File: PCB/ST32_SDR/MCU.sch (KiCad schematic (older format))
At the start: 2 parts

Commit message: add SPI in CubeMX project, add FRAM CPU PCB Project
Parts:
- removed U?: STM32F401RCTx, LQFP64, symbol STM32F401RCTx
- added C? (x4): C_Small, symbol C_Small
- added R? (x2): 0*, symbol R_Small
- added U?: STM32F401RCTx, LQFP64, symbol STM32F401RCTx
- added U?: FM24CL16B, Housings_SOIC:SOIC-8_3.9x4.9mm_Pitch1.27mm, symbol 24LC16
- added Y?: 20Mhz, symbol Crystal
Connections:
- net labels added: GND
- wire segments 30 -> 58

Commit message: Schematics update
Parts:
- removed U?: STM32F405RGTx, LQFP64, symbol STM32F405RGTx
- added C129, C130, C131, C132: 100nF, symbol C_Small
- added R94, R95: 4.7k, symbol R_Small
- C120: renamed from C?; value C_Small -> 100nF
- gave numbers to parts that had none: 8
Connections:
- net labels added: +3V3
- wire segments 58 -> 89
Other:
- moved on the sheet: U17

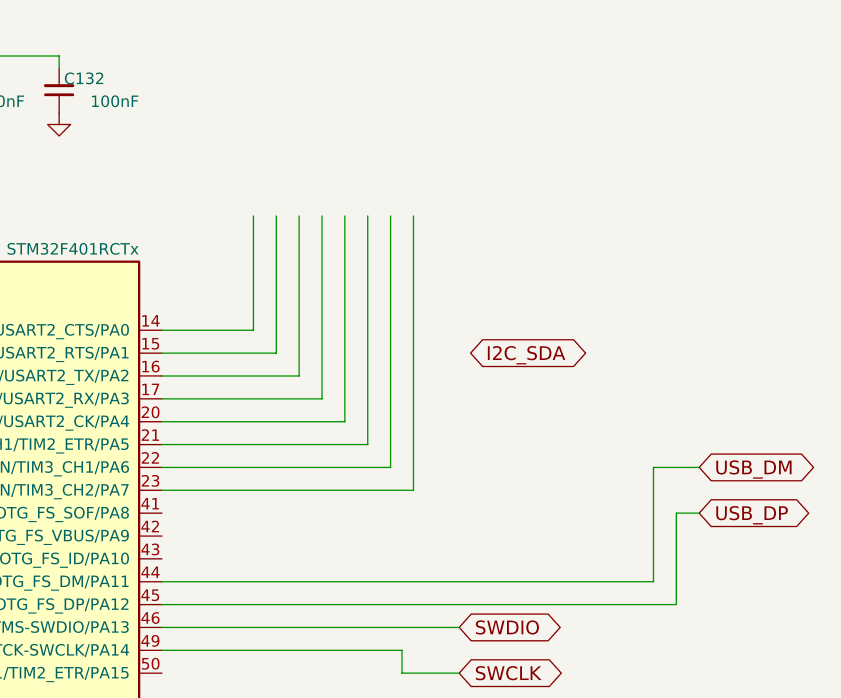
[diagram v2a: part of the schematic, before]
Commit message: MCU schematics updated LCD Interface
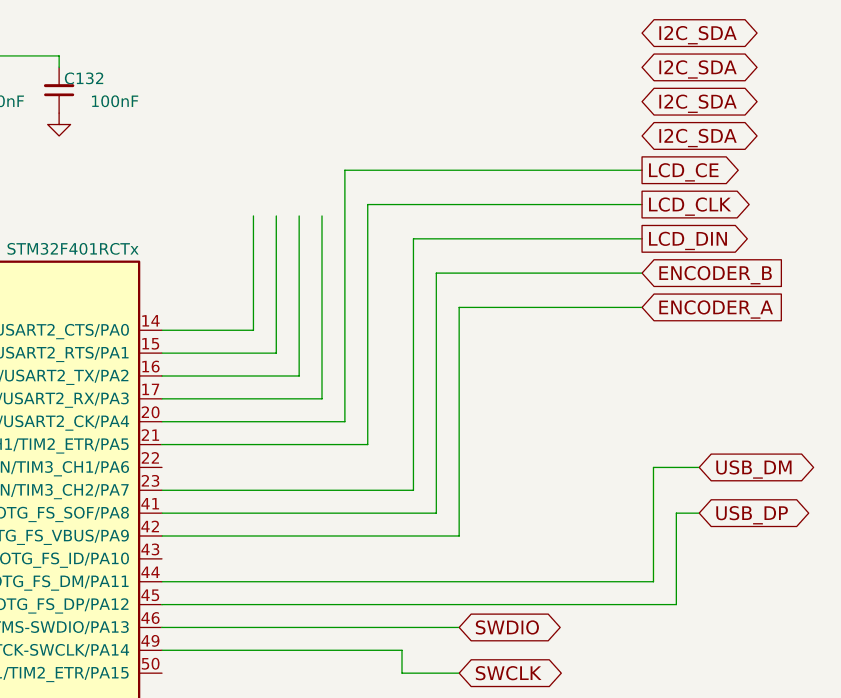
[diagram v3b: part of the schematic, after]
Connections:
- net labels added: ENCODER_A, ENCODER_B, LCD_CE, LCD_CLK, LCD_DIN
- wire segments 89 -> 96
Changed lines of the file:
@@
 LIBS:contrib
 LIBS:LCSDR
-LIBS:Logic_74xx
-LIBS:Logic_CMOS_4000
 LIBS:4ms-ic
-LIBS:Connector
 LIBS:Display
-LIBS:TRXklopik
 LIBS:LCSDR-cache
 EELAYER 25 0
@@
 	1    0    0    -1
 $EndComp
-Text GLabel 9600 1950 2    60   BiDi ~ 0
+Text GLabel 10350 850  2    60   BiDi ~ 0
 I2C_SDA
 Wire Wire Line
@@
 	8950 2150 8950 1350
 Wire Wire Line
-	8250 2250 9050 2250
-Wire Wire Line
-	9050 2250 9050 1350
-Wire Wire Line
-	8250 2350 9150 2350
-Wire Wire Line
-	9150 2350 9150 1350
-Wire Wire Line
-	8250 2450 9250 2450
-Wire Wire Line
-	9250 2450 9250 1350
+	9050 2250 8250 2250
+Wire Wire Line
+	9050 1150 9050 2250
+Wire Wire Line
+	9150 2350 8250 2350
+Wire Wire Line
+	9150 1300 9150 2350
 Wire Wire Line
 	10500 3050 10500 2650
@@
 	10400 2450 10600 2450
 Wire Wire Line
-	8250 2550 9350 2550
-Wire Wire Line
-	9350 2550 9350 1350
+	9350 2550 8250 2550
+Text GLabel 10350 700  2    60   BiDi ~ 0
+I2C_SDA
+Text GLabel 10350 550  2    60   BiDi ~ 0
+I2C_SDA
+Wire Wire Line
+	9050 1150 10350 1150
+Text GLabel 10350 1000 2    60   BiDi ~ 0
+I2C_SDA
+Text GLabel 10350 1150 2    60   Output ~ 0
+LCD_CE
+Text GLabel 10350 1300 2    60   Output ~ 0
+LCD_CLK
+Wire Wire Line
+	10350 1300 9150 1300
+Text GLabel 10350 1450 2    60   Output ~ 0
+LCD_DIN
+Wire Wire Line
+	9350 1450 9350 2550
+Wire Wire Line
+	9350 1450 10350 1450
+Wire Wire Line
+	8250 2650 9450 2650
+Wire Wire Line
+	9450 2650 9450 1600
+Wire Wire Line
+	9450 1600 10350 1600
+Wire Wire Line
+	8250 2750 9550 2750
+Text GLabel 10350 1600 2    60   Input ~ 0
+ENCODER_B
+Text GLabel 10350 1750 2    60   Input ~ 0
+ENCODER_A
+Wire Wire Line
+	10350 1750 9550 1750
+Wire Wire Line
+	9550 1750 9550 2750
 $EndSCHEMATC

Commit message: add LCD resistors
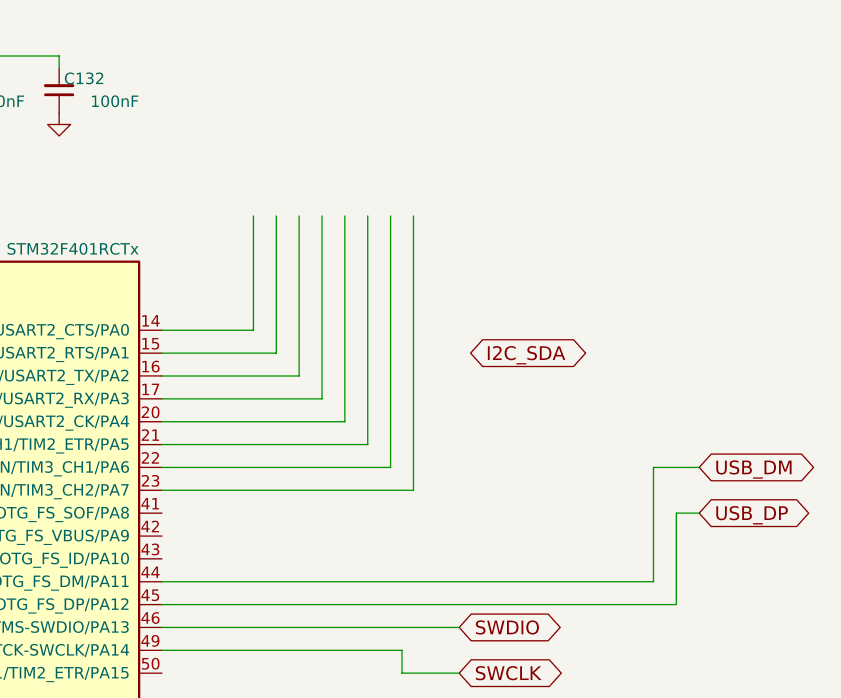
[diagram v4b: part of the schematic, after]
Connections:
- net labels removed: ENCODER_A, ENCODER_B, LCD_CE, LCD_CLK, LCD_DIN
- wire segments 96 -> 89
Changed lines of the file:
@@
 LIBS:contrib
 LIBS:LCSDR
+LIBS:Logic_74xx
+LIBS:Logic_CMOS_4000
 LIBS:4ms-ic
+LIBS:Connector
 LIBS:Display
+LIBS:TRXklopik
 LIBS:LCSDR-cache
 EELAYER 25 0
@@
 $EndComp
 $Comp
-L GND #PWR0168
+L GND #PWR171
 U 1 1 5DD64FC0
 P 5900 5900
-F 0 "#PWR0168" H 5900 5650 50  0001 C CNN
+F 0 "#PWR171" H 5900 5650 50  0001 C CNN
 F 1 "GND" H 5900 5750 50  0001 C CNN
 F 2 "" H 5900 5900 50  0001 C CNN
@@
 	5950 5350 5950 5600
 $Comp
-L GND #PWR0169
+L GND #PWR172
 U 1 1 5DD650F1
 P 6150 5450
-F 0 "#PWR0169" H 6150 5200 50  0001 C CNN
+F 0 "#PWR172" H 6150 5200 50  0001 C CNN
 F 1 "GND" H 6150 5300 50  0001 C CNN
 F 2 "" H 6150 5450 50  0001 C CNN
@@
 Connection ~ 6150 5400
 $Comp
-L GND #PWR0170
+L GND #PWR167
 U 1 1 5DD65332
 P 3250 2700
-F 0 "#PWR0170" H 3250 2450 50  0001 C CNN
+F 0 "#PWR167" H 3250 2450 50  0001 C CNN
 F 1 "GND" H 3250 2550 50  0001 C CNN
 F 2 "" H 3250 2700 50  0001 C CNN
@@
 $EndComp
 $Comp
-L GND #PWR0171
+L GND #PWR166
 U 1 1 5DD65598
 P 3050 3550
-F 0 "#PWR0171" H 3050 3300 50  0001 C CNN
+F 0 "#PWR166" H 3050 3300 50  0001 C CNN
 F 1 "GND" H 3050 3400 50  0001 C CNN
 F 2 "" H 3050 3550 50  0001 C CNN
@@
 $EndComp
 $Comp
-L GND #PWR0172
+L GND #PWR164
 U 1 1 5DD655DB
 P 2550 3550
-F 0 "#PWR0172" H 2550 3300 50  0001 C CNN
+F 0 "#PWR164" H 2550 3300 50  0001 C CNN
 F 1 "GND" H 2550 3400 50  0001 C CNN
 F 2 "" H 2550 3550 50  0001 C CNN
@@
 	2750 1850 2750 1900
 $Comp
-L GND #PWR0173
+L GND #PWR165
 U 1 1 5DD65924
 P 2750 2100
-F 0 "#PWR0173" H 2750 1850 50  0001 C CNN
+F 0 "#PWR165" H 2750 1850 50  0001 C CNN
 F 1 "GND" H 2750 1950 50  0001 C CNN
 F 2 "" H 2750 2100 50  0001 C CNN
@@
 $EndComp
 $Comp
-L GND #PWR0174
+L GND #PWR162
 U 1 1 5DD66640
 P 1450 1700
-F 0 "#PWR0174" H 1450 1450 50  0001 C CNN
+F 0 "#PWR162" H 1450 1450 50  0001 C CNN
 F 1 "GND" H 1450 1550 50  0001 C CNN
 F 2 "" H 1450 1700 50  0001 C CNN
@@
 $EndComp
 $Comp
-L GND #PWR0175
+L GND #PWR163
 U 1 1 5DD667F8
 P 1900 1550
-F 0 "#PWR0175" H 1900 1300 50  0001 C CNN
+F 0 "#PWR163" H 1900 1300 50  0001 C CNN
 F 1 "GND" H 1900 1400 50  0001 C CNN
 F 2 "" H 1900 1550 50  0001 C CNN
@@
 $EndComp
 $Comp
-L +3V3 #PWR0176
+L +3V3 #PWR169
 U 1 1 5DD9ED97
 P 4750 7450
-F 0 "#PWR0176" H 4750 7300 50  0001 C CNN
+F 0 "#PWR169" H 4750 7300 50  0001 C CNN
 F 1 "+3V3" V 4750 7700 50  0000 C CNN
 F 2 "" H 4750 7450 50  0001 C CNN
@@
 $EndComp
 $Comp
-L +3V3 #PWR0177
+L +3V3 #PWR168
 U 1 1 5DD9EE17
 P 4750 7000
-F 0 "#PWR0177" H 4750 6850 50  0001 C CNN
+F 0 "#PWR168" H 4750 6850 50  0001 C CNN
 F 1 "+3V3" V 4750 7250 50  0000 C CNN
 F 2 "" H 4750 7000 50  0001 C CNN
@@
 $EndComp
 $Comp
-L +3V3 #PWR0178
+L +3V3 #PWR161
 U 1 1 5DD9FC90
 P 1450 900
-F 0 "#PWR0178" H 1450 750 50  0001 C CNN
+F 0 "#PWR161" H 1450 750 50  0001 C CNN
 F 1 "+3V3" H 1450 1050 50  0000 C CNN
 F 2 "" H 1450 900 50  0001 C CNN
@@
 Connection ~ 1450 950
 $Comp
-L GND #PWR0179
+L GND #PWR160
 U 1 1 5DDA00B4
 P 1100 950
-F 0 "#PWR0179" H 1100 700 50  0001 C CNN
+F 0 "#PWR160" H 1100 700 50  0001 C CNN
 F 1 "GND" H 1100 800 50  0001 C CNN
 F 2 "" H 1100 950 50  0001 C CNN
@@
 $EndComp
 $Comp
-L +3V3 #PWR0180
+L +3V3 #PWR170
 U 1 1 5DDA012B
 P 5550 1300
-F 0 "#PWR0180" H 5550 1150 50  0001 C CNN
+F 0 "#PWR170" H 5550 1150 50  0001 C CNN
 F 1 "+3V3" V 5550 1550 50  0000 C CNN
 F 2 "" H 5550 1300 50  0001 C CNN
@@
 $EndComp
 $Comp
-L +3V3 #PWR0181
+L +3V3 #PWR173
 U 1 1 5DDA0C93
 P 6600 650
-F 0 "#PWR0181" H 6600 500 50  0001 C CNN
+F 0 "#PWR173" H 6600 500 50  0001 C CNN
 F 1 "+3V3" V 6600 900 50  0000 C CNN
 F 2 "" H 6600 650 50  0001 C CNN
@@
 Connection ~ 6800 650
 $Comp
-L GND #PWR0182
+L GND #PWR174
 U 1 1 5DDA0E68
 P 6800 900
-F 0 "#PWR0182" H 6800 650 50  0001 C CNN
+F 0 "#PWR174" H 6800 650 50  0001 C CNN
 F 1 "GND" H 6800 750 50  0001 C CNN
 F 2 "" H 6800 900 50  0001 C CNN
@@
 $EndComp
 $Comp
-L GND #PWR0183
+L GND #PWR175
 U 1 1 5DDA0EDC
 P 7300 900
-F 0 "#PWR0183" H 7300 650 50  0001 C CNN
+F 0 "#PWR175" H 7300 650 50  0001 C CNN
 F 1 "GND" H 7300 750 50  0001 C CNN
 F 2 "" H 7300 900 50  0001 C CNN
@@
 $EndComp
 $Comp
-L GND #PWR0184
+L GND #PWR176
 U 1 1 5DDA0F4B
 P 7800 900
-F 0 "#PWR0184" H 7800 650 50  0001 C CNN
+F 0 "#PWR176" H 7800 650 50  0001 C CNN
 F 1 "GND" H 7800 750 50  0001 C CNN
 F 2 "" H 7800 900 50  0001 C CNN
@@
 	1    0    0    -1
 $EndComp
-Text GLabel 10350 850  2    60   BiDi ~ 0
+Text GLabel 9600 1950 2    60   BiDi ~ 0
 I2C_SDA
 Wire Wire Line
@@
 	8950 2150 8950 1350
 Wire Wire Line
-	9050 2250 8250 2250
-Wire Wire Line
-	9050 1150 9050 2250
-Wire Wire Line
-	9150 2350 8250 2350
-Wire Wire Line
-	9150 1300 9150 2350
+	8250 2250 9050 2250
+Wire Wire Line
+	9050 2250 9050 1350
+Wire Wire Line
+	8250 2350 9150 2350
+Wire Wire Line
+	9150 2350 9150 1350
+Wire Wire Line
+	8250 2450 9250 2450
+Wire Wire Line
+	9250 2450 9250 1350
 Wire Wire Line
 	10500 3050 10500 2650
@@
 	10400 2450 10600 2450
 Wire Wire Line
-	9350 2550 8250 2550
-Text GLabel 10350 700  2    60   BiDi ~ 0
-I2C_SDA
-Text GLabel 10350 550  2    60   BiDi ~ 0
-I2C_SDA
-Wire Wire Line
-	9050 1150 10350 1150
-Text GLabel 10350 1000 2    60   BiDi ~ 0
-I2C_SDA
-Text GLabel 10350 1150 2    60   Output ~ 0
-LCD_CE
-Text GLabel 10350 1300 2    60   Output ~ 0
-LCD_CLK
-Wire Wire Line
-	10350 1300 9150 1300
-Text GLabel 10350 1450 2    60   Output ~ 0
-LCD_DIN
-Wire Wire Line
-	9350 1450 9350 2550
-Wire Wire Line
-	9350 1450 10350 1450
-Wire Wire Line
-	8250 2650 9450 2650
-Wire Wire Line
-	9450 2650 9450 1600
-Wire Wire Line
-	9450 1600 10350 1600
-Wire Wire Line
-	8250 2750 9550 2750
-Text GLabel 10350 1600 2    60   Input ~ 0
-ENCODER_B
-Text GLabel 10350 1750 2    60   Input ~ 0
-ENCODER_A
-Wire Wire Line
-	10350 1750 9550 1750
-Wire Wire Line
-	9550 1750 9550 2750
+	8250 2550 9350 2550
+Wire Wire Line
+	9350 2550 9350 1350
 $EndSCHEMATC

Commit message: fix MCU
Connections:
- net labels added: ENCODER_A, ENCODER_B, LCD_CE, LCD_CLK, LCD_DC, LCD_DIN
- wire segments 89 -> 97
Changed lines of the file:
@@
 LIBS:contrib
 LIBS:LCSDR
-LIBS:Logic_74xx
-LIBS:Logic_CMOS_4000
 LIBS:4ms-ic
-LIBS:Connector
 LIBS:Display
-LIBS:TRXklopik
 LIBS:LCSDR-cache
 EELAYER 25 0
@@
 $EndComp
 $Comp
-L GND #PWR171
+L GND #PWR0168
 U 1 1 5DD64FC0
 P 5900 5900
-F 0 "#PWR171" H 5900 5650 50  0001 C CNN
+F 0 "#PWR0168" H 5900 5650 50  0001 C CNN
 F 1 "GND" H 5900 5750 50  0001 C CNN
 F 2 "" H 5900 5900 50  0001 C CNN
@@
 	5950 5350 5950 5600
 $Comp
-L GND #PWR172
+L GND #PWR0169
 U 1 1 5DD650F1
 P 6150 5450
-F 0 "#PWR172" H 6150 5200 50  0001 C CNN
+F 0 "#PWR0169" H 6150 5200 50  0001 C CNN
 F 1 "GND" H 6150 5300 50  0001 C CNN
 F 2 "" H 6150 5450 50  0001 C CNN
@@
 Connection ~ 6150 5400
 $Comp
-L GND #PWR167
+L GND #PWR0170
 U 1 1 5DD65332
 P 3250 2700
-F 0 "#PWR167" H 3250 2450 50  0001 C CNN
+F 0 "#PWR0170" H 3250 2450 50  0001 C CNN
 F 1 "GND" H 3250 2550 50  0001 C CNN
 F 2 "" H 3250 2700 50  0001 C CNN
@@
 $EndComp
 $Comp
-L GND #PWR166
+L GND #PWR0171
 U 1 1 5DD65598
 P 3050 3550
-F 0 "#PWR166" H 3050 3300 50  0001 C CNN
+F 0 "#PWR0171" H 3050 3300 50  0001 C CNN
 F 1 "GND" H 3050 3400 50  0001 C CNN
 F 2 "" H 3050 3550 50  0001 C CNN
@@
 $EndComp
 $Comp
-L GND #PWR164
+L GND #PWR0172
 U 1 1 5DD655DB
 P 2550 3550
-F 0 "#PWR164" H 2550 3300 50  0001 C CNN
+F 0 "#PWR0172" H 2550 3300 50  0001 C CNN
 F 1 "GND" H 2550 3400 50  0001 C CNN
 F 2 "" H 2550 3550 50  0001 C CNN
@@
 	2750 1850 2750 1900
 $Comp
-L GND #PWR165
+L GND #PWR0173
 U 1 1 5DD65924
 P 2750 2100
-F 0 "#PWR165" H 2750 1850 50  0001 C CNN
+F 0 "#PWR0173" H 2750 1850 50  0001 C CNN
 F 1 "GND" H 2750 1950 50  0001 C CNN
 F 2 "" H 2750 2100 50  0001 C CNN
@@
 $EndComp
 $Comp
-L GND #PWR162
+L GND #PWR0174
 U 1 1 5DD66640
 P 1450 1700
-F 0 "#PWR162" H 1450 1450 50  0001 C CNN
+F 0 "#PWR0174" H 1450 1450 50  0001 C CNN
 F 1 "GND" H 1450 1550 50  0001 C CNN
 F 2 "" H 1450 1700 50  0001 C CNN
@@
 $EndComp
 $Comp
-L GND #PWR163
+L GND #PWR0175
 U 1 1 5DD667F8
 P 1900 1550
-F 0 "#PWR163" H 1900 1300 50  0001 C CNN
+F 0 "#PWR0175" H 1900 1300 50  0001 C CNN
 F 1 "GND" H 1900 1400 50  0001 C CNN
 F 2 "" H 1900 1550 50  0001 C CNN
@@
 $EndComp
 $Comp
-L +3V3 #PWR169
+L +3V3 #PWR0176
 U 1 1 5DD9ED97
 P 4750 7450
-F 0 "#PWR169" H 4750 7300 50  0001 C CNN
+F 0 "#PWR0176" H 4750 7300 50  0001 C CNN
 F 1 "+3V3" V 4750 7700 50  0000 C CNN
 F 2 "" H 4750 7450 50  0001 C CNN
@@
 $EndComp
 $Comp
-L +3V3 #PWR168
+L +3V3 #PWR0177
 U 1 1 5DD9EE17
 P 4750 7000
-F 0 "#PWR168" H 4750 6850 50  0001 C CNN
+F 0 "#PWR0177" H 4750 6850 50  0001 C CNN
 F 1 "+3V3" V 4750 7250 50  0000 C CNN
 F 2 "" H 4750 7000 50  0001 C CNN
@@
 $EndComp
 $Comp
-L +3V3 #PWR161
+L +3V3 #PWR0178
 U 1 1 5DD9FC90
 P 1450 900
-F 0 "#PWR161" H 1450 750 50  0001 C CNN
+F 0 "#PWR0178" H 1450 750 50  0001 C CNN
 F 1 "+3V3" H 1450 1050 50  0000 C CNN
 F 2 "" H 1450 900 50  0001 C CNN
@@
 Connection ~ 1450 950
 $Comp
-L GND #PWR160
+L GND #PWR0179
 U 1 1 5DDA00B4
 P 1100 950
-F 0 "#PWR160" H 1100 700 50  0001 C CNN
+F 0 "#PWR0179" H 1100 700 50  0001 C CNN
 F 1 "GND" H 1100 800 50  0001 C CNN
 F 2 "" H 1100 950 50  0001 C CNN
@@
 $EndComp
 $Comp
-L +3V3 #PWR170
+L +3V3 #PWR0180
 U 1 1 5DDA012B
 P 5550 1300
-F 0 "#PWR170" H 5550 1150 50  0001 C CNN
+F 0 "#PWR0180" H 5550 1150 50  0001 C CNN
 F 1 "+3V3" V 5550 1550 50  0000 C CNN
 F 2 "" H 5550 1300 50  0001 C CNN
@@
 $EndComp
 $Comp
-L +3V3 #PWR173
+L +3V3 #PWR0181
 U 1 1 5DDA0C93
 P 6600 650
-F 0 "#PWR173" H 6600 500 50  0001 C CNN
+F 0 "#PWR0181" H 6600 500 50  0001 C CNN
 F 1 "+3V3" V 6600 900 50  0000 C CNN
 F 2 "" H 6600 650 50  0001 C CNN
@@
 Connection ~ 6800 650
 $Comp
-L GND #PWR174
+L GND #PWR0182
 U 1 1 5DDA0E68
 P 6800 900
-F 0 "#PWR174" H 6800 650 50  0001 C CNN
+F 0 "#PWR0182" H 6800 650 50  0001 C CNN
 F 1 "GND" H 6800 750 50  0001 C CNN
 F 2 "" H 6800 900 50  0001 C CNN
@@
 $EndComp
 $Comp
-L GND #PWR175
+L GND #PWR0183
 U 1 1 5DDA0EDC
 P 7300 900
-F 0 "#PWR175" H 7300 650 50  0001 C CNN
+F 0 "#PWR0183" H 7300 650 50  0001 C CNN
 F 1 "GND" H 7300 750 50  0001 C CNN
 F 2 "" H 7300 900 50  0001 C CNN
@@
 $EndComp
 $Comp
-L GND #PWR176
+L GND #PWR0184
 U 1 1 5DDA0F4B
 P 7800 900
-F 0 "#PWR176" H 7800 650 50  0001 C CNN
+F 0 "#PWR0184" H 7800 650 50  0001 C CNN
 F 1 "GND" H 7800 750 50  0001 C CNN
 F 2 "" H 7800 900 50  0001 C CNN
@@
 	1    0    0    -1
 $EndComp
-Text GLabel 9600 1950 2    60   BiDi ~ 0
+Text GLabel 10350 850  2    60   BiDi ~ 0
 I2C_SDA
 Wire Wire Line
@@
 	8850 2050 8850 1350
 Wire Wire Line
-	8250 2150 8950 2150
-Wire Wire Line
-	8950 2150 8950 1350
-Wire Wire Line
-	8250 2250 9050 2250
-Wire Wire Line
-	9050 2250 9050 1350
-Wire Wire Line
-	8250 2350 9150 2350
-Wire Wire Line
-	9150 2350 9150 1350
-Wire Wire Line
-	8250 2450 9250 2450
-Wire Wire Line
-	9250 2450 9250 1350
+	8950 2150 8250 2150
+Wire Wire Line
+	8950 1000 8950 2150
+Wire Wire Line
+	9050 2250 8250 2250
+Wire Wire Line
+	9050 1150 9050 2250
+Wire Wire Line
+	9150 2350 8250 2350
+Wire Wire Line
+	9150 1300 9150 2350
 Wire Wire Line
 	10500 3050 10500 2650
@@
 	10400 2450 10600 2450
 Wire Wire Line
-	8250 2550 9350 2550
-Wire Wire Line
-	9350 2550 9350 1350
+	9350 2550 8250 2550
+Text GLabel 10350 700  2    60   BiDi ~ 0
+I2C_SDA
+Text GLabel 10350 550  2    60   BiDi ~ 0
+I2C_SDA
+Wire Wire Line
+	9050 1150 10350 1150
+Text GLabel 10350 1000 2    60   Output ~ 0
+LCD_DC
+Text GLabel 10350 1150 2    60   Output ~ 0
+LCD_CE
+Text GLabel 10350 1300 2    60   Output ~ 0
+LCD_CLK
+Wire Wire Line
+	10350 1300 9150 1300
+Text GLabel 10350 1450 2    60   Output ~ 0
+LCD_DIN
+Wire Wire Line
+	9350 1450 9350 2550
+Wire Wire Line
+	9350 1450 10350 1450
+Wire Wire Line
+	8250 2650 9450 2650
+Wire Wire Line
+	9450 2650 9450 1600
+Wire Wire Line
+	9450 1600 10350 1600
+Wire Wire Line
+	8250 2750 9550 2750
+Text GLabel 10350 1600 2    60   Input ~ 0
+ENCODER_B
+Text GLabel 10350 1750 2    60   Input ~ 0
+ENCODER_A
+Wire Wire Line
+	10350 1750 9550 1750
+Wire Wire Line
+	9550 1750 9550 2750
+Wire Wire Line
+	8950 1000 10350 1000
 $EndSCHEMATC

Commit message: update schematics
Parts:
- removed R94, R95: 4.7k, symbol R_Small
- C118: value C_Small -> 100nF
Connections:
- net labels added: ATT, BAND0, BAND1, BAND2, BAND3, I_IN_M1, I_IN_M2, KEY_A, KEY_B, KEY_C, KEY_CW, KEY_D, KEY_MENU, LCD_LIGHT, LCD_RESET, LINE_OUT_LEFT_MCU, LINE_OUT_RIGHT_MCU, MCU_RESET, PREAMP, PTT_IN, Q_IN_M1, Q_IN_M2, S-metr, TX1, TX2, UART_RX, UART_TX
- wire segments 97 -> 161
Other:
- moved on the sheet: C117, C119, Y1
